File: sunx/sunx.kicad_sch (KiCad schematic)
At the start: 9 parts, among them J1 Conn_01x05_Socket, J2 Conn_01x04_Socket, U1 HT7333-3-SOT89, con1 Conn_01x08_MountingPin

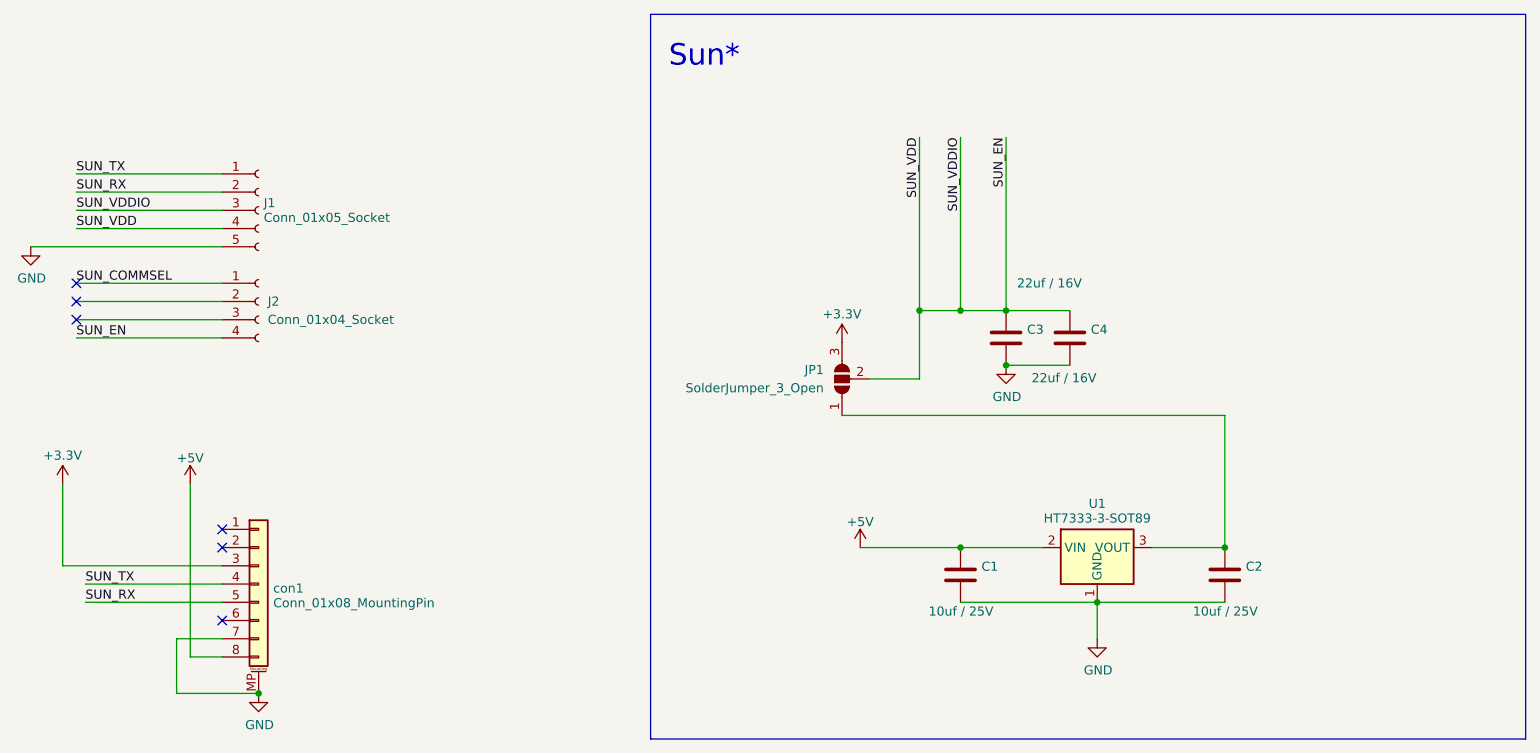
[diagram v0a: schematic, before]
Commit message: WIP v2.1: AP2112K-3.3 LDO, 0R power-select links, revised placement
Carried over from Bitbucket branch V2.1 (commit 9a7380c) with the same
import-only adjustments as main. Changes on top of v2.0, per the source
commits: LDO HT7333 -> AP2112K-3.3, solder jumper JP1 replaced by 0R links
R1/R2 (R1 DNP), bulk tantalum C5 added then marked DNP ('big cap is not
needed'), silkscreen marking updated, parts moved clear of the connector.
No production set - untested and unreleased.
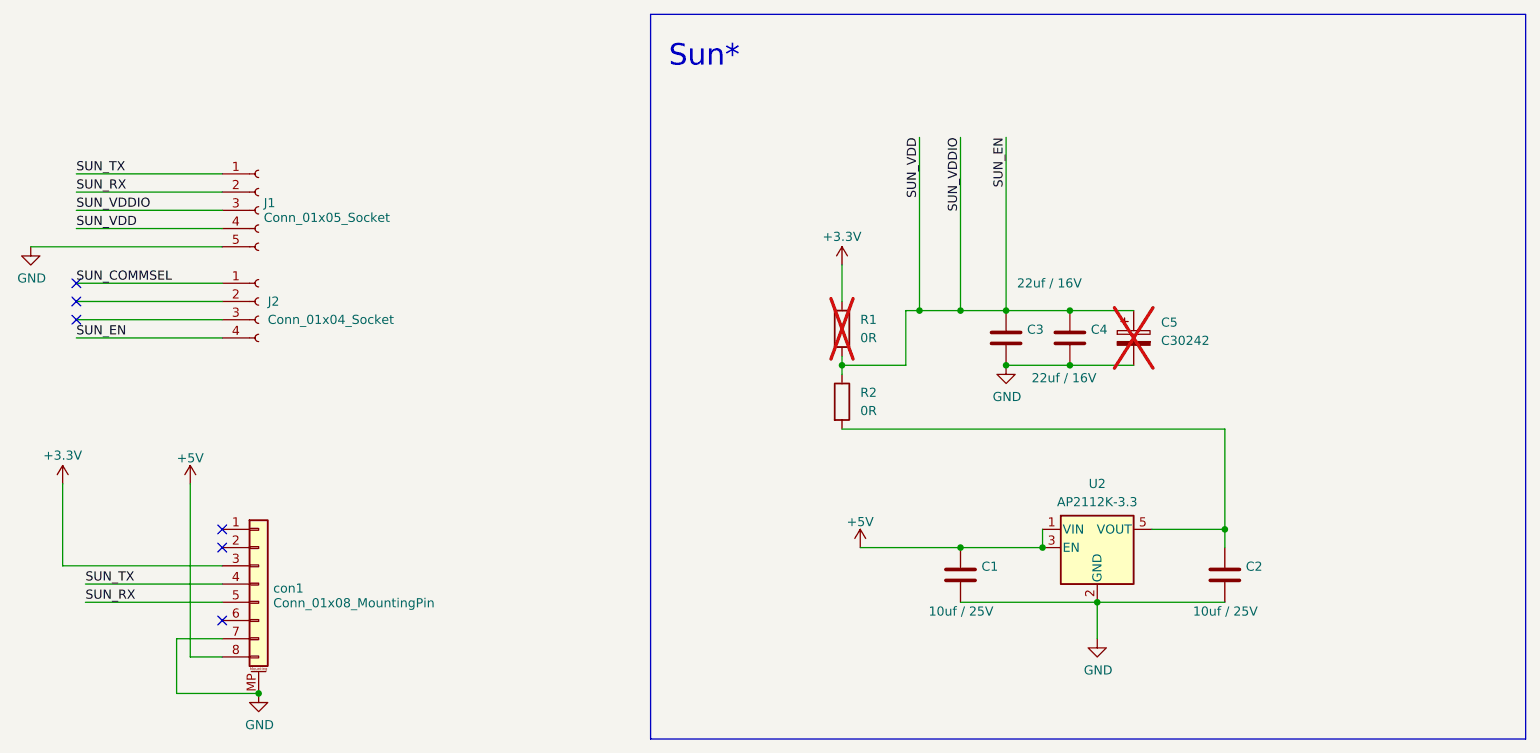
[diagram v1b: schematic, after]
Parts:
- removed JP1: SolderJumper_3_Open, Jumper:SolderJumper-3_P1.3mm_Bridged12_RoundedPad1.0x1.5mm_NumberLabels, symbol Jumper:SolderJumper_3_Open
- removed U1: HT7333-3-SOT89, Package_TO_SOT_SMD:SOT-89-3, symbol Regulator_Linear:HT75xx-1-SOT89
- added C5: C30242, Capacitor_Tantalum_SMD:CP_EIA-3528-21_Kemet-B, symbol Device:C_Polarized
- added R1, R2: 0R, Resistor_SMD:R_0603_1608Metric, symbol Device:R
- added U2: AP2112K-3.3, Package_TO_SOT_SMD:SOT-23-5, symbol Regulator_Linear:AP2112K-3.3
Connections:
- net +3.3V: now also R1.1
- net +5V: now also U2.1 (VIN), U2.3 (EN)
- net GND: now also C5.2, U2.2 (GND)
- net SUN_EN: now also C5.1, R1.2, R2.1
- net at C2.1: now also R2.2, U2.5 (VOUT)
